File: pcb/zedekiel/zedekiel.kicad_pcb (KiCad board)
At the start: 2 copper layers, 165 parts, among them K1 KEYSW, K10 KEYSW, K11 KEYSW, K12 KEYSW, K13 KEYSW, K14 KEYSW, K15 KEYSW, K16 KEYSW, K17 KEYSW, K18 KEYSW, K19 KEYSW, K2 KEYSW, K20 KEYSW, K21 KEYSW, K22 KEYSW, K23 KEYSW, K24 KEYSW, K25 KEYSW, K26 KEYSW, K27 KEYSW, K28 KEYSW, K29 KEYSW, K3 KEYSW, K30 KEYSW, K31 KEYSW, K32 KEYSW, K33 KEYSW, K34 KEYSW, K35 KEYSW, K36 KEYSW, K37 KEYSW, K38 KEYSW, K39 KEYSW, K4 KEYSW, K40 KEYSW, K41 KEYSW, K42 KEYSW, K43 KEYSW, K44 KEYSW, K45 KEYSW, K46 KEYSW, K47 KEYSW, K48 KEYSW, K49 KEYSW, K5 KEYSW, K50 KEYSW, K51 KEYSW, K52 KEYSW, K53 KEYSW, K54 KEYSW, K55 KEYSW, K56 KEYSW, K57 KEYSW, K58 KEYSW, K59 KEYSW, K6 KEYSW, K60 KEYSW, K61 KEYSW, K62 KEYSW, K63 KEYSW, K64 KEYSW, K65 KEYSW, K66 KEYSW, K7 KEYSW, K8 KEYSW, K9 KEYSW, SW1 SW_PUSH, U1 ATmega16U4-AU_(modified), X1 16MHz

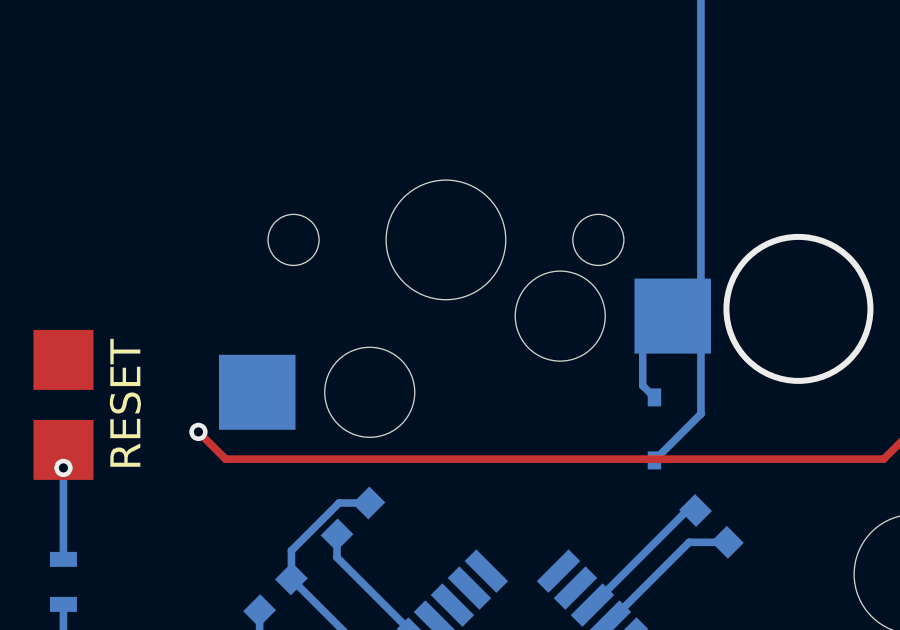
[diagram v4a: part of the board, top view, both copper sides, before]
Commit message: Fixed another socket
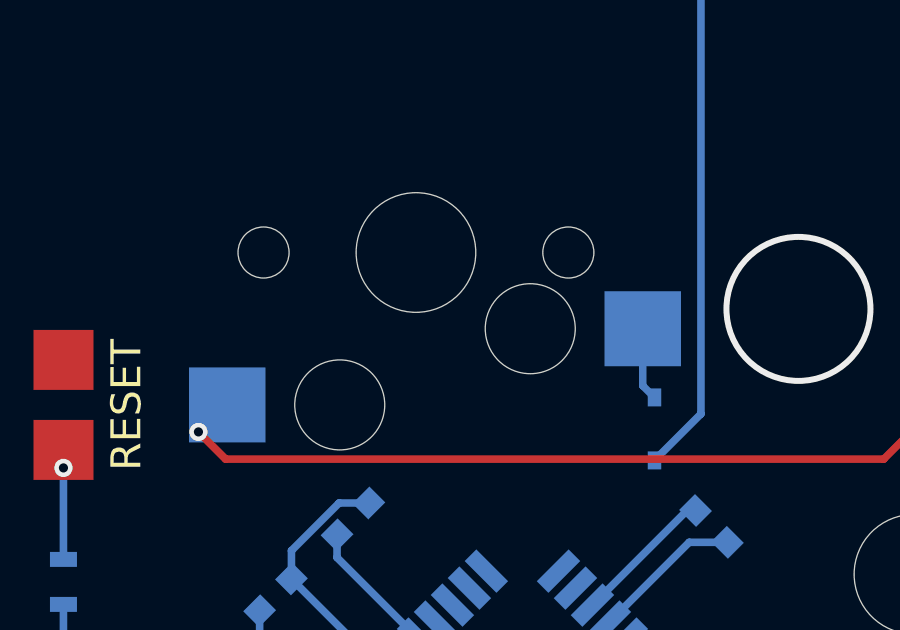
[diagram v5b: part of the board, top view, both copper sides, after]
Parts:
- moved K43 1.08 mm to (34.6, 86.9)
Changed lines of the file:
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@@
     (47 F.CrtYd user)
     (48 B.Fab user hide)
-    (49 F.Fab user hide)
+    (49 F.Fab user)
   )
   (setup
@@
       (effects (font (size 1 1) (thickness 0.15)))
     )
+    (fp_arc (start 3.81 4.445) (end 3.81 6.985) (angle -90) (layer B.SilkS) (width 0.15))
+    (fp_arc (start 0 0) (end 0 2.54) (angle -75.96375653) (layer B.SilkS) (width 0.15))
+    (fp_arc (start 3.81 4.445) (end 3.81 6.985) (angle -90) (layer B.Fab) (width 0.12))
+    (fp_arc (start 0 0) (end 0 2.54) (angle -75.96375653) (layer B.Fab) (width 0.12))
+    (fp_line (start 6.9 -6.9) (end -6.9 -6.9) (layer Eco2.User) (width 0.15))
+    (fp_line (start -6.9 6.9) (end 6.9 6.9) (layer Eco2.User) (width 0.15))
+    (fp_line (start -6.9 6.9) (end -6.9 -6.9) (layer Eco2.User) (width 0.15))
+    (fp_line (start 6.9 -6.9) (end 6.9 6.9) (layer Eco2.User) (width 0.15))
+    (fp_line (start 7.5 7.5) (end -7.5 7.5) (layer F.Fab) (width 0.15))
+    (fp_line (start -7.5 7.5) (end -7.5 -7.5) (layer F.Fab) (width 0.15))
+    (fp_line (start -7.5 -7.5) (end 7.5 -7.5) (layer F.Fab) (width 0.15))
+    (fp_line (start 7.5 -7.5) (end 7.5 7.5) (layer F.Fab) (width 0.15))
+    (fp_line (start 6.35 1.016) (end 6.35 0.635) (layer B.SilkS) (width 0.15))
+    (fp_line (start -5.08 3.556) (end -5.08 2.54) (layer B.SilkS) (width 0.15))
+    (fp_line (start -5.08 2.54) (end 0 2.54) (layer B.SilkS) (width 0.15))
+    (fp_line (start 2.464162 0.635) (end 4.191 0.635) (layer B.SilkS) (width 0.15))
+    (fp_line (start 5.969 0.635) (end 6.35 0.635) (layer B.SilkS) (width 0.15))
+    (fp_line (start 6.35 4.445) (end 6.35 4.064) (layer B.SilkS) (width 0.15))
+    (fp_line (start 3.81 6.985) (end -5.08 6.985) (layer B.SilkS) (width 0.15))
+    (fp_line (start -5.08 6.985) (end -5.08 6.604) (layer B.SilkS) (width 0.15))
+    (fp_line (start 6.35 0.635) (end 2.54 0.635) (layer B.Fab) (width 0.12))
+    (fp_line (start 6.35 0.635) (end 6.35 4.445) (layer B.Fab) (width 0.12))
+    (fp_line (start 3.81 6.985) (end -5.08 6.985) (layer B.Fab) (width 0.12))
+    (fp_line (start -5.08 6.985) (end -5.08 2.54) (layer B.Fab) (width 0.12))
+    (fp_line (start -5.08 2.54) (end 0 2.54) (layer B.Fab) (width 0.12))
+    (fp_line (start -5.08 6.35) (end -7.62 6.35) (layer B.Fab) (width 0.12))
+    (fp_line (start -7.62 6.35) (end -7.62 3.81) (layer B.Fab) (width 0.12))
+    (fp_line (start -7.62 3.81) (end -5.08 3.81) (layer B.Fab) (width 0.12))
+    (fp_line (start 6.35 1.27) (end 8.89 1.27) (layer B.Fab) (width 0.12))
+    (fp_line (start 8.89 1.27) (end 8.89 3.81) (layer B.Fab) (width 0.12))
+    (fp_line (start 8.89 3.81) (end 6.35 3.81) (layer B.Fab) (width 0.12))
+    (fp_line (start -19 -9.5) (end 19 -9.5) (layer Dwgs.User) (width 0.12))
+    (fp_line (start 19 -9.5) (end 19 9.5) (layer Dwgs.User) (width 0.12))
+    (fp_line (start -19 9.5) (end 19 9.5) (layer Dwgs.User) (width 0.12))
     (fp_line (start -19 -9.5) (end -19 9.5) (layer Dwgs.User) (width 0.12))
-    (fp_line (start -19 9.5) (end 19 9.5) (layer Dwgs.User) (width 0.12))
-    (fp_line (start 19 -9.5) (end 19 9.5) (layer Dwgs.User) (width 0.12))
-    (fp_line (start -19 -9.5) (end 19 -9.5) (layer Dwgs.User) (width 0.12))
-    (fp_line (start 8.89 3.81) (end 6.35 3.81) (layer B.Fab) (width 0.12))
-    (fp_line (start 8.89 1.27) (end 8.89 3.81) (layer B.Fab) (width 0.12))
-    (fp_line (start 6.35 1.27) (end 8.89 1.27) (layer B.Fab) (width 0.12))
-    (fp_line (start -7.62 3.81) (end -5.08 3.81) (layer B.Fab) (width 0.12))
-    (fp_line (start -7.62 6.35) (end -7.62 3.81) (layer B.Fab) (width 0.12))
-    (fp_line (start -5.08 6.35) (end -7.62 6.35) (layer B.Fab) (width 0.12))
-    (fp_line (start -5.08 2.54) (end 0 2.54) (layer B.Fab) (width 0.12))
-    (fp_line (start -5.08 6.985) (end -5.08 2.54) (layer B.Fab) (width 0.12))
-    (fp_line (start 3.81 6.985) (end -5.08 6.985) (layer B.Fab) (width 0.12))
-    (fp_line (start 6.35 0.635) (end 6.35 4.445) (layer B.Fab) (width 0.12))
-    (fp_line (start 6.35 0.635) (end 2.54 0.635) (layer B.Fab) (width 0.12))
-    (fp_line (start -5.08 6.985) (end -5.08 6.604) (layer B.SilkS) (width 0.15))
-    (fp_line (start 3.81 6.985) (end -5.08 6.985) (layer B.SilkS) (width 0.15))
-    (fp_line (start 6.35 4.445) (end 6.35 4.064) (layer B.SilkS) (width 0.15))
-    (fp_line (start 5.969 0.635) (end 6.35 0.635) (layer B.SilkS) (width 0.15))
-    (fp_line (start 2.464162 0.635) (end 4.191 0.635) (layer B.SilkS) (width 0.15))
-    (fp_line (start -5.08 2.54) (end 0 2.54) (layer B.SilkS) (width 0.15))
-    (fp_line (start -5.08 3.556) (end -5.08 2.54) (layer B.SilkS) (width 0.15))
-    (fp_line (start 6.35 1.016) (end 6.35 0.635) (layer B.SilkS) (width 0.15))
-    (fp_line (start 7.5 -7.5) (end 7.5 7.5) (layer F.Fab) (width 0.15))
-    (fp_line (start -7.5 -7.5) (end 7.5 -7.5) (layer F.Fab) (width 0.15))
-    (fp_line (start -7.5 7.5) (end -7.5 -7.5) (layer F.Fab) (width 0.15))
-    (fp_line (start 7.5 7.5) (end -7.5 7.5) (layer F.Fab) (width 0.15))
-    (fp_line (start 6.9 -6.9) (end 6.9 6.9) (layer Eco2.User) (width 0.15))
-    (fp_line (start -6.9 6.9) (end -6.9 -6.9) (layer Eco2.User) (width 0.15))
-    (fp_line (start -6.9 6.9) (end 6.9 6.9) (layer Eco2.User) (width 0.15))
-    (fp_line (start 6.9 -6.9) (end -6.9 -6.9) (layer Eco2.User) (width 0.15))
-    (fp_arc (start 0 0) (end 0 2.54) (angle -75.96375653) (layer B.Fab) (width 0.12))
-    (fp_arc (start 3.81 4.445) (end 3.81 6.985) (angle -90) (layer B.Fab) (width 0.12))
-    (fp_arc (start 0 0) (end 0 2.54) (angle -75.96375653) (layer B.SilkS) (width 0.15))
-    (fp_arc (start 3.81 4.445) (end 3.81 6.985) (angle -90) (layer B.SilkS) (width 0.15))
+    (pad 1 smd rect (at -6.29 5.08 180) (size 2.55 2.5) (layers B.Cu B.Paste B.Mask)
+      (net 90 /R5))
+    (pad "" np_thru_hole circle (at -2.54 5.08 180) (size 3 3) (drill 3) (layers *.Cu *.Mask))
+    (pad "" np_thru_hole circle (at 3.81 2.54 180) (size 3 3) (drill 3) (layers *.Cu *.Mask))
+    (pad "" np_thru_hole circle (at 0 0 180) (size 3.9878 3.9878) (drill 3.9878) (layers *.Cu *.Mask))
+    (pad "" np_thru_hole circle (at -5.08 0 180) (size 1.7018 1.7018) (drill 1.7018) (layers *.Cu *.Mask))
+    (pad "" np_thru_hole circle (at 5.08 0 180) (size 1.7018 1.7018) (drill 1.7018) (layers *.Cu *.Mask))
     (pad 2 smd rect (at 7.56 2.54 180) (size 2.55 2.5) (layers B.Cu B.Paste B.Mask)
       (net 76 "Net-(D57-Pad1)"))
-    (pad "" np_thru_hole circle (at 5.08 0 180) (size 1.7018 1.7018) (drill 1.7018) (layers *.Cu *.Mask))
-    (pad "" np_thru_hole circle (at -5.08 0 180) (size 1.7018 1.7018) (drill 1.7018) (layers *.Cu *.Mask))
-    (pad "" np_thru_hole circle (at 0 0 180) (size 3.9878 3.9878) (drill 3.9878) (layers *.Cu *.Mask))
-    (pad "" np_thru_hole circle (at 3.81 2.54 180) (size 3 3) (drill 3) (layers *.Cu *.Mask))
-    (pad "" np_thru_hole circle (at -2.54 5.08 180) (size 3 3) (drill 3) (layers *.Cu *.Mask))
-    (pad 1 smd rect (at -6.29 5.08 180) (size 2.55 2.5) (layers B.Cu B.Paste B.Mask)
-      (net 90 /R5))
   )
   (module custom:Kailh_socket_MX_1.50U (layer F.Cu)
@@
   )
   (module custom:Kailh_socket_MX_1.50U (layer F.Cu)
-    (at 35.65 86.5)
+    (at 34.65 86.92)
     (descr "MX-style keyswitch with Kailh socket mount")
     (tags MX,cherry,gateron,kailh,pg1511,socket)

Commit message: Pads
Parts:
- added TP1: TestPoint, custom:single-pad, B.Cu at (56.9, 23.9)
- added TP10: TestPoint, custom:single-pad, B.Cu at (22.9, 86.4)
- added TP2: TestPoint, custom:single-pad, B.Cu at (59.4, 23.9)
- added TP3: TestPoint, custom:single-pad, B.Cu at (61.9, 23.9)
- added TP4: TestPoint, custom:single-pad, B.Cu at (64.4, 23.9)
- added TP5: TestPoint, custom:single-pad, B.Cu at (22.9, 77.4)
- added TP6: TestPoint, custom:single-pad, B.Cu at (22.9, 74.4)
- added TP7: TestPoint, custom:single-pad, B.Cu at (30.4, 112.4)
- added TP8: TestPoint, custom:single-pad, B.Cu at (22.9, 80.8)
- added TP9: TestPoint, custom:single-pad, B.Cu at (22.9, 83.6)
- moved R6 15.1 mm to (45.0, 112.6), turned to 45 degrees
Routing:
- net /R5: track 336.1 -> 362.4 mm
- net Net-(R5-Pad2): track 2.23 -> 23.2 mm, vias 0 -> 2
- net Net-(R4-Pad2): track 2.23 -> 19.0 mm, vias 0 -> 2
- net VCC: track 33.9 -> 43.7 mm
- net GND: track 13.6 -> 5.06 mm, vias 0 -> 45
- net Net-(R6-Pad1): track 9.43 -> 5.84 mm
- net (no net): vias 8 -> 20
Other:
- board text added: "+"
- board text added: "-"
- board text added: "D+"
- board text added: "D-"

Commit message: Progress, I guess..
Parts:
- removed the TP6 at (22.9, 74.4)
- added TP6: TestPoint, custom:single-pad, B.Cu at (22.9, 68.4)
- added TP6: TestPoint, custom:single-pad, B.Cu at (22.9, 70.9)
- added TP6: TestPoint, custom:single-pad, B.Cu at (22.9, 73.7)
- moved TP7 34.6 mm to (22.9, 78.7)
- moved C5 16.6 mm to (31.2, 113.0), turned to 135 degrees
- moved R6 11.4 mm to (33.6, 113.0), turned to 135 degrees
- moved TP5 1.25 mm to (22.9, 76.2)
- moved C7 0.78 mm to (43.7, 96.0)
- moved TP8 0.60 mm to (22.9, 81.4)
- moved TP9 0.30 mm to (22.9, 83.9)
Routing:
- net /C13: track 92.3 -> 339.4 mm, vias 0 -> 2
- net /C12: track 95.1 -> 312.5 mm, vias 0 -> 2
- net VCC: track 43.7 -> 149.8 mm, vias 0 -> 3
- net /R1: track 259.8 -> 350.2 mm
- net /C4: track 87.7 -> 155.5 mm, vias 0 -> 2
- net /R2: track 276.5 -> 343.5 mm, vias 14 -> 16
- net /C3: track 67.7 -> 124.7 mm, vias 0 -> 2
- net MISO: track 0.00 -> 27.2 mm
- net MOSI: track 0.00 -> 25.0 mm
- net SCLK: track 0.00 -> 22.1 mm
- net Net-(R6-Pad1): track 5.84 -> 0.00 mm
- net Net-(C2-Pad1): track 3.07 -> 7.64 mm
- net /R5: track 362.4 -> 363.3 mm
- net GND: track 5.06 -> 4.32 mm

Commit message: working on better routing
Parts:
- moved D7 2.37 mm to (158.5, 39.1), turned to 270 degrees
- turned REF** to 45 degrees
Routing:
- net /C13: track 339.4 -> 90.5 mm, vias 2 -> 0
- net /C12: track 312.5 -> 93.2 mm, vias 2 -> 0
- net /C4: track 155.5 -> 87.9 mm, vias 2 -> 0
- net /C3: track 124.7 -> 67.8 mm, vias 2 -> 0
- net /C7: track 93.0 -> 88.0 mm
- net /C1: track 67.8 -> 63.8 mm
- net /C14: track 89.9 -> 88.1 mm
- net /C8: track 91.0 -> 92.2 mm
- net Net-(D7-Pad1): track 7.34 -> 6.63 mm
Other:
- net class EasyEDA: clearance 0.2 -> 0.3
